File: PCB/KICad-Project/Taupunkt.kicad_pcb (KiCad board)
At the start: 2 copper layers, 90 x 104 mm, 21 parts, among them J1 DC PWR, J2 DHT22 inside, J3 DHT22 outside, J4 20x4 LCD, J5 D1 MINI - RTC, J6 SD-Card, J7 Relay Fan1, J7 Relay Fan2, SW1 RST-Switch, SW2 ModeSwitch

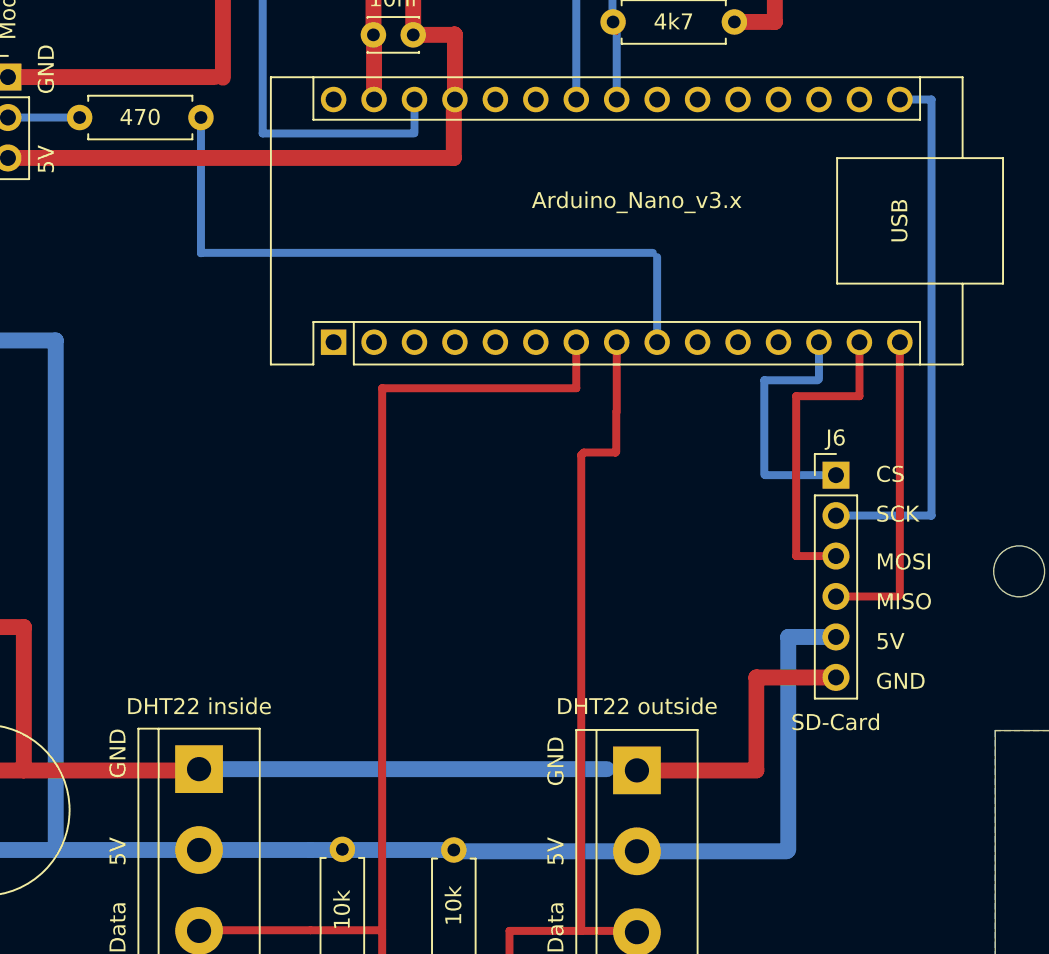
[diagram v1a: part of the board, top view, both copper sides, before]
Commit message: Fixed silkscreen (switched inside and outside sensors to match assigned pins in code), slightly moved away the sd card pinheader.
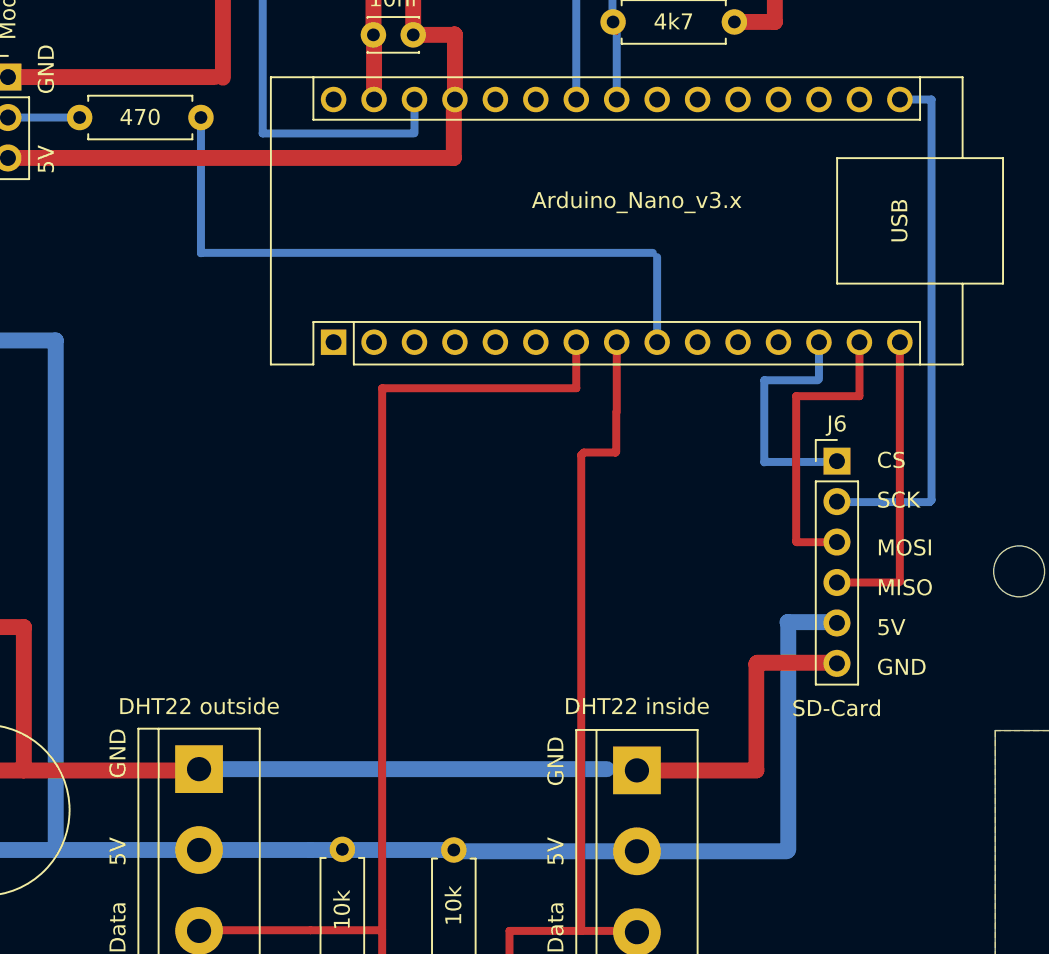
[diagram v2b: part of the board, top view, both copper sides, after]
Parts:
- J2: value DHT22 inside -> DHT22 outside
- J3: value DHT22 outside -> DHT22 inside
- moved J6 0.88 mm to (120.1, 128.1)
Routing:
- net /<NO NET>: track 263.9 -> 265.0 mm
- net /SCK: track 34.1 -> 33.2 mm
- net /GND: track 236.7 -> 237.6 mm
- net /MISO: track 19.9 -> 19.0 mm
- net /MOSI: track 19.9 -> 19.1 mm
- net /CS: track 16.2 -> 15.5 mm
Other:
- board text added: "Taupunktregelung mit Logger v0.4 https://github.com/MakeMagazinDE/Taupunktluefter"
- board text removed: "Taupunktregelung mit Logger v0.3 https://github.com/MakeMagazinDE/Taupunktluefter"
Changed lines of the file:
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@@
 			)
 		)
-		(property "Value" "DHT22 outside"
+		(property "Value" "DHT22 inside"
 			(at -4 0 180)
 			(layer "F.SilkS")
@@
 	(footprint "Connector_PinHeader_2.54mm:PinHeader_1x06_P2.54mm_Vertical"
 		(layer "F.Cu")
-		(at 120 128.96)
+		(at 120.06 128.08)
 		(descr "Through hole straight pin header, 1x06, 2.54mm pitch, single row")
 		(tags "Through hole pin header THT 1x06 2.54mm single row")
@@
 			)
 		)
-		(property "Value" "DHT22 inside"
+		(property "Value" "DHT22 outside"
 			(at -3.92 0 180)
 			(layer "F.SilkS")
@@
 		(layer "Edge.Cuts")
 	)
-	(gr_text "Taupunktregelung mit Logger v0.3\nhttps://github.com/MakeMagazinDE/Taupunktluefter\n\n"
+	(gr_text "Taupunktregelung mit Logger v0.4\nhttps://github.com/MakeMagazinDE/Taupunktluefter\n\n"
 		(at 113.31 136.97 0)
 		(layer "B.SilkS")
@@
 	)
 	(gr_text "MOSI"
-		(at 122.5 135 0)
+		(at 122.56 134.12 0)
 		(layer "F.SilkS")
 		(effects
@@
 	)
 	(gr_text "CS"
-		(at 122.5 129.5 0)
+		(at 122.56 128.62 0)
 		(layer "F.SilkS")
 		(effects
@@
 	)
 	(gr_text "SCK"
-		(at 122.5 132 0)
+		(at 122.56 131.12 0)
 		(layer "F.SilkS")
 		(effects
@@
 	)
 	(gr_text "MISO\n"
-		(at 122.5 137.5 0)
+		(at 122.56 136.62 0)
 		(layer "F.SilkS")
 		(effects
@@
 	)
 	(gr_text "5V"
-		(at 122.5 140 0)
+		(at 122.56 139.12 0)
 		(layer "F.SilkS")
 		(effects
@@
 	)
 	(gr_text "GND"
-		(at 122.5 142.5 0)
+		(at 122.56 141.62 0)
 		(layer "F.SilkS")
 		(effects
@@
 	)
 	(segment
-		(start 115 147.5)
-		(end 107.5 147.5)
-		(width 1)
-		(layer "F.Cu")
-		(net 3)
-	)
-	(segment
 		(start 80.97 103.96)
 		(end 68 103.96)
@@
 	)
 	(segment
+		(start 120.02 140.74)
+		(end 115.07 140.74)
+		(width 1)
+		(layer "F.Cu")
+		(net 3)
+	)
+	(segment
+		(start 115 140.81)
+		(end 115 147.5)
+		(width 1)
+		(layer "F.Cu")
+		(net 3)
+	)
+	(segment
 		(start 90.87 97)
 		(end 81.455 97)
@@
 	)
 	(segment
-		(start 115 141.66)
-		(end 115 147.5)
+		(start 115 147.5)
+		(end 107.5 147.5)
 		(width 1)
 		(layer "F.Cu")
@@
 	)
 	(segment
+		(start 120.06 140.78)
+		(end 120.02 140.74)
+		(width 1)
+		(layer "F.Cu")
+		(net 3)
+	)
+	(segment
 		(start 69 138.5)
 		(end 69 147.5)
@@
 	)
 	(segment
-		(start 120 141.66)
-		(end 115 141.66)
-		(width 1)
-		(layer "F.Cu")
-		(net 3)
-	)
-	(segment
 		(start 108.5 92)
 		(end 90.94 92)
@@
 	)
 	(segment
+		(start 115.07 140.74)
+		(end 115 140.81)
+		(width 1)
+		(layer "F.Cu")
+		(net 3)
+	)
+	(segment
 		(start 90.95 101.31)
 		(end 90.99 101.35)
@@
 	)
 	(segment
-		(start 118.86 123)
-		(end 115.5 123)
+		(start 115.52 128.13)
+		(end 120.01 128.13)
 		(width 0.5)
 		(layer "B.Cu")
@@
 	)
 	(segment
-		(start 115.5 123)
-		(end 115.5 128.92)
+		(start 118.86 123)
+		(end 115.5 123)
 		(width 0.5)
 		(layer "B.Cu")
@@
 	)
 	(segment
-		(start 115.5 128.92)
-		(end 115.54 128.96)
-		(width 0.2)
+		(start 120.01 128.13)
+		(end 120.06 128.08)
+		(width 0.5)
+		(layer "B.Cu")
+		(net 13)
+	)
+	(segment
+		(start 115.5 123)
+		(end 115.5 128.15)
+		(width 0.5)
 		(layer "B.Cu")
 		(net 13)
 	)
 	(segment
-		(start 115.54 128.96)
-		(end 120 128.96)
+		(start 115.5 128.15)
+		(end 115.52 128.13)
 		(width 0.5)
 		(layer "B.Cu")
@@
 	)
 	(segment
+		(start 120.06 130.62)
+		(end 120.09 130.65)
+		(width 0.5)
+		(layer "B.Cu")
+		(net 24)
+	)
+	(segment
+		(start 120.09 130.65)
+		(end 125.88 130.65)
+		(width 0.5)
+		(layer "B.Cu")
+		(net 24)
+	)
+	(segment
 		(start 126 105.37)
 		(end 124.01 105.37)
@@
 	)
 	(segment
-		(start 120 131.5)
-		(end 126 131.5)
+		(start 126 130.53)
+		(end 126 105.37)
 		(width 0.5)
 		(layer "B.Cu")
@@
 	)
 	(segment
-		(start 126 131.5)
-		(end 126 105.37)
+		(start 125.88 130.65)
+		(end 126 130.53)
 		(width 0.5)
 		(layer "B.Cu")
@@
 	)
 	(segment
-		(start 123.92 136.58)
-		(end 124.01 136.49)
-		(width 0.2)
+		(start 124.01 135.63)
+		(end 123.94 135.7)
+		(width 0.5)
 		(layer "F.Cu")
 		(net 27)
 	)
 	(segment
-		(start 124.01 136.49)
-		(end 124.01 120.61)
+		(start 123.94 135.7)
+		(end 120.06 135.7)
 		(width 0.5)
 		(layer "F.Cu")
@@
 	)
 	(segment
-		(start 120 136.58)
-		(end 123.92 136.58)
+		(start 124.01 135.63)
+		(end 124.01 120.61)
 		(width 0.5)
 		(layer "F.Cu")
@@
 	)
 	(segment
+		(start 120.01 138.19)
+		(end 120.06 138.24)
+		(width 1)
+		(layer "B.Cu")
+		(net 28)
+	)
+	(segment
 		(start 71 152.5)
 		(end 71 120.5)
@@
 	)
 	(segment
-		(start 117 139.12)
-		(end 120 139.12)
+		(start 117 138.23)
+		(end 116.96 138.19)
+		(width 1)
+		(layer "B.Cu")
+		(net 28)
+	)
+	(segment
+		(start 117 152.5)
+		(end 117 138.23)
 		(width 1)
 		(layer "B.Cu")
@@
 	)
 	(segment
-		(start 117 152.5)
-		(end 117 139.12)
-		(width 1)
-		(layer "B.Cu")
-		(net 28)
-	)
-	(segment
 		(start 95.5 152.5)
 		(end 87.04 152.5)
@@
 	)
 	(segment
+		(start 116.96 138.19)
+		(end 120.01 138.19)
+		(width 1)
+		(layer "B.Cu")
+		(net 28)
+	)
+	(segment
 		(start 80 152.5)
 		(end 86.96 152.5)
@@
 	)
 	(segment
-		(start 117.5 124)
-		(end 121.47 124)
+		(start 121.47 124)
+		(end 121.47 120.61)
 		(width 0.5)
 		(layer "F.Cu")
@@
 	)
 	(segment
-		(start 117.5 134.04)
-		(end 117.5 124)
+		(start 120.06 133.16)
+		(end 120.05 133.17)
 		(width 0.5)
 		(layer "F.Cu")
@@
 	)
 	(segment
-		(start 120 134.04)
-		(end 117.5 134.04)
+		(start 120.05 133.17)
+		(end 117.54 133.17)
 		(width 0.5)
 		(layer "F.Cu")
@@
 	)
 	(segment
-		(start 121.47 124)
-		(end 121.47 120.61)
+		(start 117.5 124)
+		(end 121.47 124)
+		(width 0.5)
+		(layer "F.Cu")
+		(net 29)
+	)
+	(segment
+		(start 117.54 133.17)
+		(end 117.5 133.13)
+		(width 0.5)
+		(layer "F.Cu")
+		(net 29)
+	)
+	(segment
+		(start 117.5 133.13)
+		(end 117.5 124)
 		(width 0.5)
 		(layer "F.Cu")
